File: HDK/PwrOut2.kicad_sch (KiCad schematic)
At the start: 7 parts, among them J301 PwrOut_{5v}, J302 PwrOut_{5v}, J303 PwrOut_{9v}, J304 PwrOut_{9v}, J305 PwrOut_{12v}, J306 PwrOut_{12v}, J307 PwrOut_{2}

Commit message: updated sch
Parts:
- J301, J302, J303, J304, J305, J306, J307: footprint Connector_Molex:Molex_Mini-Fit_Jr_5566-02A_2x01_P4.20mm_Vertical -> (none)
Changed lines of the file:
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@@
 	(title_block
 		(title "Power Distribution Unit")
-		(date "2024-07-17")
+		(date "2024-07-29")
 		(rev "1")
 		(company "Scott CJX")
@@
 			)
 		)
-		(property "Footprint" "Connector_Molex:Molex_Mini-Fit_Jr_5566-02A_2x01_P4.20mm_Vertical"
+		(property "Footprint" ""
 			(at 114.3 25.4 0)
 			(effects
@@
 			)
 		)
-		(property "Footprint" "Connector_Molex:Molex_Mini-Fit_Jr_5566-02A_2x01_P4.20mm_Vertical"
+		(property "Footprint" ""
 			(at 114.3 53.34 0)
 			(effects
@@
 			)
 		)
-		(property "Footprint" "Connector_Molex:Molex_Mini-Fit_Jr_5566-02A_2x01_P4.20mm_Vertical"
+		(property "Footprint" ""
 			(at 114.3 62.23 0)
 			(effects
@@
 			)
 		)
-		(property "Footprint" "Connector_Molex:Molex_Mini-Fit_Jr_5566-02A_2x01_P4.20mm_Vertical"
+		(property "Footprint" ""
 			(at 114.3 36.83 0)
 			(effects
@@
 			)
 		)
-		(property "Footprint" "Connector_Molex:Molex_Mini-Fit_Jr_5566-02A_2x01_P4.20mm_Vertical"
+		(property "Footprint" ""
 			(at 114.3 30.48 0)
 			(effects
@@
 			)
 		)
-		(property "Footprint" "Connector_Molex:Molex_Mini-Fit_Jr_5566-02A_2x01_P4.20mm_Vertical"
+		(property "Footprint" ""
 			(at 114.3 41.91 0)
 			(effects
@@
 			)
 		)
-		(property "Footprint" "Connector_Molex:Molex_Mini-Fit_Jr_5566-02A_2x01_P4.20mm_Vertical"
+		(property "Footprint" ""
 			(at 114.3 48.26 0)
 			(effects

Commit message: updated sch
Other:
- note added: "Power Connectors (Computing)"
- note removed: "Power Connectors (Propulsion & Actuators)"
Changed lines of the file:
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@@
 		)
 	)
-	(text "Power Connectors (Propulsion & Actuators)"
+	(text "Power Connectors (Computing)"
 		(exclude_from_sim no)
 		(at 20.32 19.05 0)

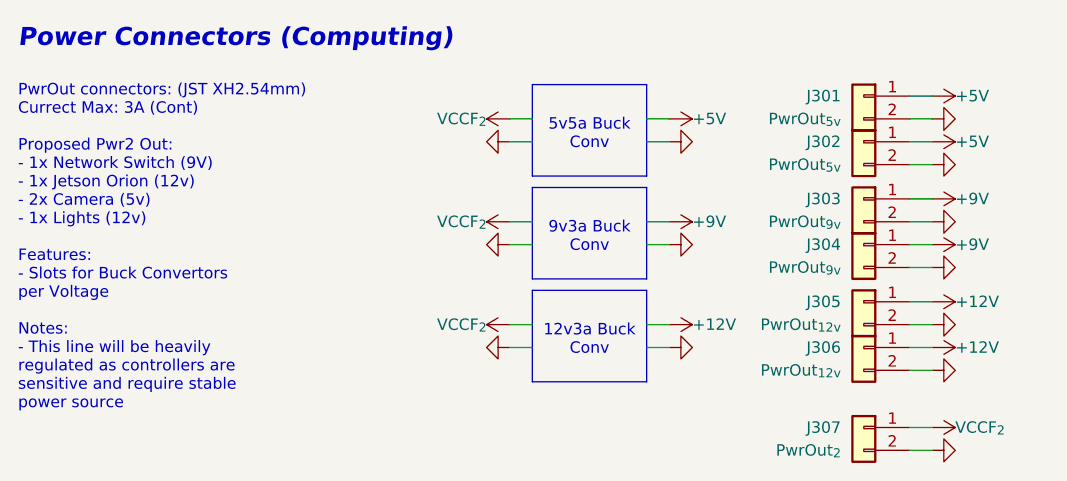
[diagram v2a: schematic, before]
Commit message: added connectors
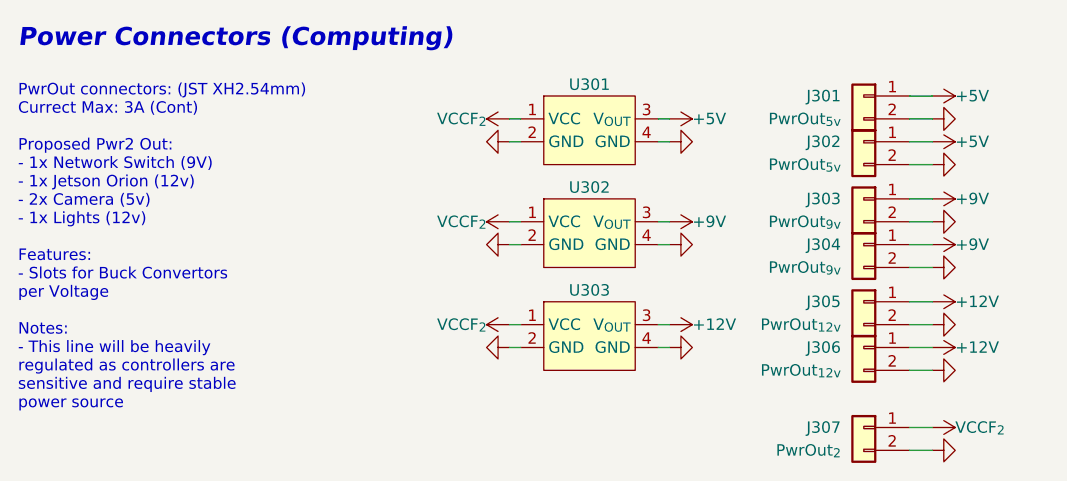
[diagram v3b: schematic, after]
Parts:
- added U301, U302, U303: ~, symbol mecatron-kicad-rsc:buck_convertor
- J307: footprint (none) -> mecatron-kicad-footprints:AMASS_XT30PW-F_1x02_P2.50mm_Horizontal
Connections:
- net +12V: now also U303.3 (V_{OUT})
- net +5V: now also U301.3 (V_{OUT})
- net +9V: now also U302.3 (V_{OUT})
- net GND: now also U301.2 (GND), U301.4 (GND), U302.2 (GND), U302.4 (GND), U303.2 (GND), U303.4 (GND)
- net VCCF_{2}: now also U301.1 (VCC), U302.1 (VCC), U303.1 (VCC)
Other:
- note removed: "12v3a Buck Conv"
- note removed: "5v5a Buck Conv"
- note removed: "9v3a Buck Conv"
